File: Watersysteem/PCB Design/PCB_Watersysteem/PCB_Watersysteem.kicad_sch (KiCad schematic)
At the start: 69 parts, among them J1 12V ingang, J10 LED Water Level, J11 LED Nutrient Level, J12 Height Nutrients, J13 Height Mixer, J2 TTL Connector, J21 Voedingstoffen 1, J3 ReferentieProbe, J4 Voedingstoffen 2, J5 Voedingstoffen 3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

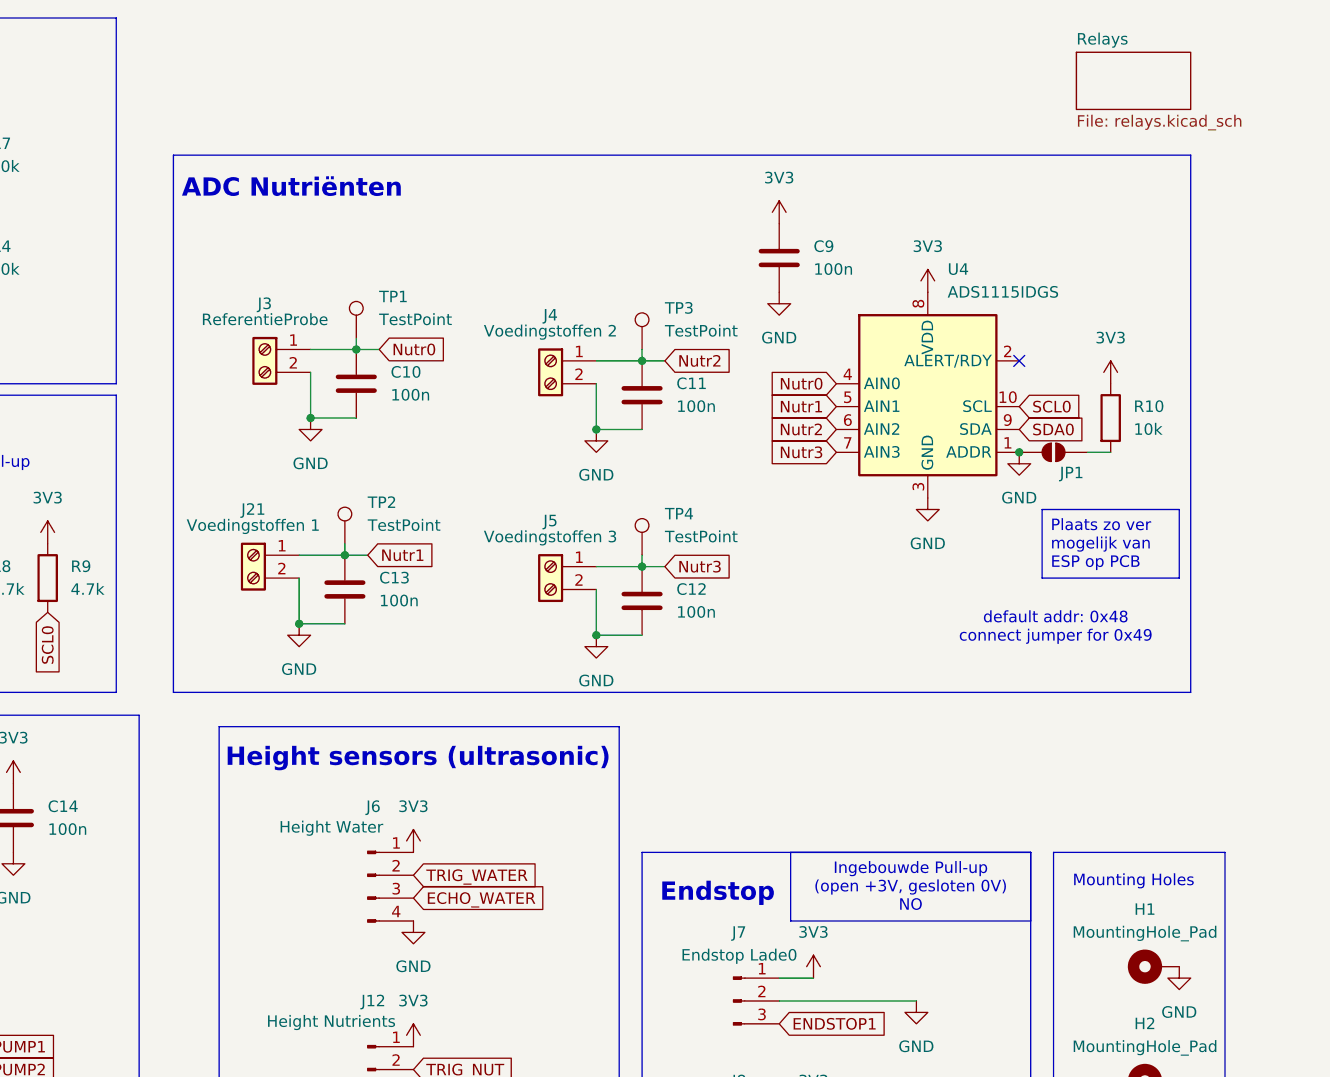
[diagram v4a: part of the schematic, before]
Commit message: Update PCB
BNC Connectoren ingevoegd, extra footprints
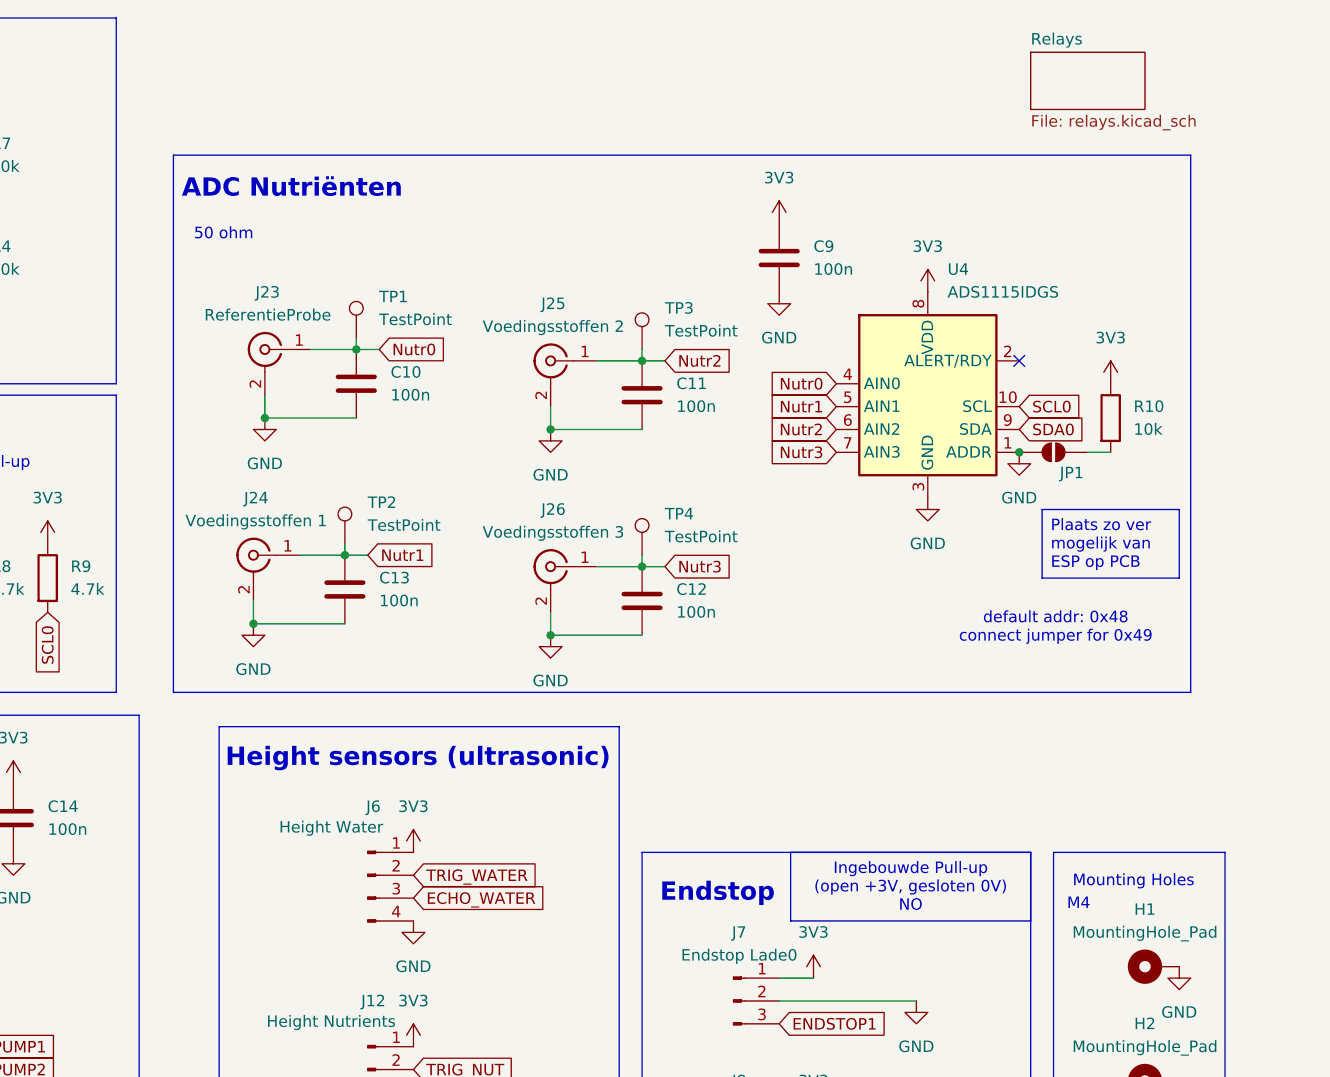
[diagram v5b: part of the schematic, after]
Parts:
- removed J21: Voedingstoffen 1, symbol Connector:Screw_Terminal_01x02
- removed J3: ReferentieProbe, symbol Connector:Screw_Terminal_01x02
- removed J4: Voedingstoffen 2, symbol Connector:Screw_Terminal_01x02
- removed J5: Voedingstoffen 3, symbol Connector:Screw_Terminal_01x02
- added J23: ReferentieProbe, Connector_Coaxial:BNC_Amphenol_B6252HB-NPP3G-50_Horizontal, symbol Connector:Conn_Coaxial
- added J24: Voedingsstoffen 1, Connector_Coaxial:BNC_Amphenol_B6252HB-NPP3G-50_Horizontal, symbol Connector:Conn_Coaxial
- added J25: Voedingsstoffen 2, Connector_Coaxial:BNC_Amphenol_B6252HB-NPP3G-50_Horizontal, symbol Connector:Conn_Coaxial
- added J26: Voedingsstoffen 3, Connector_Coaxial:BNC_Amphenol_B6252HB-NPP3G-50_Horizontal, symbol Connector:Conn_Coaxial
- C1, C2: footprint (none) -> Capacitor_SMD:CP_Elec_6.3x3.9
- C4: footprint (none) -> Capacitor_Tantalum_SMD:CP_EIA-3528-12_Kemet-T_Pad1.50x2.35mm_HandSolder
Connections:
- net GND: now also J23.2 (Ext), J24.2 (Ext), J25.2 (Ext), J26.2 (Ext)
- net Nutr0: now also J23.1 (In)
- net Nutr1: now also J24.1 (In)
- net Nutr2: now also J25.1 (In)
- net Nutr3: now also J26.1 (In)
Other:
- note added: "50 ohm"
- note added: "M4"

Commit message: Update PCB
alle footprints staan correct, alles in PCB geïmporteert
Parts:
- H1, H2, H3, H4: footprint MountingHole:MountingHole_4.3mm_M4_DIN965_Pad_TopBottom -> MountingHole:MountingHole_3.2mm_M3_Pad_TopBottom
- J1: footprint (none) -> TerminalBlock_Phoenix:TerminalBlock_Phoenix_PT-1,5-2-5.0-H_1x02_P5.00mm_Horizontal
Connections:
- net 12V: now also U2.2 (IN+); no longer U2.3 (IN+), U2.4 (IN+)
- net 5V: now also U2.3 (OUT+); no longer U2.5 (OUT+), U2.6 (OUT+)
- net GND: now also U2.4 (OUT-); no longer U2.2 (IN-), U2.7 (OUT-), U2.8 (OUT-)
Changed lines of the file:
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@@
 	)
 	(junction
+		(at 72.39 177.8)
+		(diameter 0)
+		(color 0 0 0 0)
+	)
+	(junction
 		(at 128.27 177.8)
 		(diameter 0)
@@
 	)
 	(junction
-		(at 53.34 186.69)
-		(diameter 0)
-		(color 0 0 0 0)
-	)
-	(junction
 		(at 92.71 133.35)
 		(diameter 0)
@@
 	)
 	(junction
-		(at 71.12 177.8)
-		(diameter 0)
-		(color 0 0 0 0)
-	)
-	(junction
 		(at 130.81 177.8)
 		(diameter 0)
@@
 	)
 	(junction
-		(at 71.12 186.69)
-		(diameter 0)
-		(color 0 0 0 0)
-	)
-	(junction
 		(at 187.96 50.8)
 		(diameter 0)
@@
 	)
 	(junction
-		(at 53.34 177.8)
-		(diameter 0)
-		(color 0 0 0 0)
-	)
-	(junction
 		(at 113.03 35.56)
 		(diameter 0)
@@
 		(color 0 0 0 0)
 	)
-	(junction
-		(at 73.66 177.8)
-		(diameter 0)
-		(color 0 0 0 0)
-	)
 	(no_connect
 		(at 63.5 60.96)
@@
 	(wire
 		(pts
-			(xy 73.66 177.8) (xy 74.93 177.8)
-		)
-		(stroke
-			(width 0)
-			(type default)
-		)
-	)
-	(wire
-		(pts
 			(xy 82.55 177.8) (xy 77.47 177.8)
 		)
@@
 	(wire
 		(pts
-			(xy 71.12 177.8) (xy 71.12 180.34)
-		)
-		(stroke
-			(width 0)
-			(type default)
-		)
-	)
-	(wire
-		(pts
 			(xy 234.95 139.7) (xy 250.19 139.7)
 		)
@@
 	(wire
 		(pts
-			(xy 71.12 184.15) (xy 71.12 186.69)
-		)
-		(stroke
-			(width 0)
-			(type default)
-		)
-	)
-	(wire
-		(pts
 			(xy 96.52 154.94) (xy 100.33 154.94)
 		)
@@
 	(wire
 		(pts
-			(xy 53.34 177.8) (xy 53.34 180.34)
-		)
-		(stroke
-			(width 0)
-			(type default)
-		)
-	)
-	(wire
-		(pts
 			(xy 187.96 49.53) (xy 187.96 50.8)
 		)
@@
 	(wire
 		(pts
+			(xy 71.12 184.15) (xy 71.12 186.69)
+		)
+		(stroke
+			(width 0)
+			(type default)
+		)
+	)
+	(wire
+		(pts
 			(xy 92.71 128.27) (xy 104.14 128.27)
 		)
@@
 	(wire
 		(pts
-			(xy 71.12 177.8) (xy 73.66 177.8)
+			(xy 71.12 177.8) (xy 72.39 177.8)
+		)
+		(stroke
+			(width 0)
+			(type default)
+		)
+	)
+	(wire
+		(pts
+			(xy 72.39 177.8) (xy 74.93 177.8)
 		)
 		(stroke
@@
 	)
 	(symbol
-		(lib_id "power:PWR_FLAG")
-		(at 29.21 184.15 90)
-		(unit 1)
-		(exclude_from_sim no)
-		(in_bom yes)
-		(on_board yes)
-		(dnp no)
-		(fields_autoplaced yes)
-		(property "Reference" "#FLG01"
-			(at 27.305 184.15 0)
-			(effects
-				(font
-					(size 1.27 1.27)
-				)
-				(hide yes)
-			)
-		)
-		(property "Value" "PWR_FLAG"
-			(at 25.4 184.1499 90)
-			(effects
-				(font
-					(size 1.27 1.27)
-				)
-				(justify left)
-			)
-		)
-		(property "Footprint" ""
-			(at 29.21 184.15 0)
-			(effects
-				(font
-					(size 1.27 1.27)
-				)
-				(hide yes)
-			)
-		)
-		(property "Datasheet" "~"
-			(at 29.21 184.15 0)
-			(effects
-				(font
-					(size 1.27 1.27)
-				)
-				(hide yes)
-			)
-		)
-		(property "Description" "Special symbol for telling ERC where power comes from"
-			(at 29.21 184.15 0)
-			(effects
-				(font
-					(size 1.27 1.27)
-				)
-				(hide yes)
-			)
-		)
-		(pin "1"
-		)
-		(instances
-			(project ""
-				(path "/de0b8b90-8fde-4ab1-b1b1-e85d44454ecd"
-					(reference "#FLG01")
-					(unit 1)
-				)
-			)
-		)
-	)
-	(symbol
 		(lib_id "power:GND")
 		(at 19.05 35.56 0)
@@
 			)
 		)
-		(property "Footprint" "MountingHole:MountingHole_4.3mm_M4_DIN965_Pad_TopBottom"
+		(property "Footprint" "MountingHole:MountingHole_3.2mm_M3_Pad_TopBottom"
 			(at 276.86 144.78 0)
 			(effects
@@
 	(symbol
 		(lib_id "power:VCC")
-		(at 73.66 177.8 0)
+		(at 72.39 177.8 0)
 		(unit 1)
 		(exclude_from_sim no)
@@
 		(fields_autoplaced yes)
 		(property "Reference" "#PWR06"
-			(at 73.66 181.61 0)
+			(at 72.39 181.61 0)
 			(effects
 				(font
@@
 		)
 		(property "Value" "5V"
-			(at 73.66 172.72 0)
+			(at 72.39 172.72 0)
 			(effects
 				(font
@@
 		)
 		(property "Footprint" ""
-			(at 73.66 177.8 0)
+			(at 72.39 177.8 0)
 			(effects
 				(font
@@
 		)
 		(property "Datasheet" ""
-			(at 73.66 177.8 0)
+			(at 72.39 177.8 0)
 			(effects
 				(font
@@
 		)
 		(property "Description" "Power symbol creates a global label with name \"VCC\""
-			(at 73.66 177.8 0)
+			(at 72.39 177.8 0)
 			(effects
 				(font
@@
 			)
 		)
+		(property "Sim.Pins" "1=K 2=A"
+			(at 148.59 177.8 0)
+			(effects
+				(font
+					(size 1.27 1.27)
+				)
+				(hide yes)
+			)
+		)
 		(pin "2"
 		)
@@
 	)
 	(symbol
+		(lib_name "LED_1")
 		(lib_id "Device:LED")
 		(at 130.81 78.74 90)
@@
 			)
 		)
+		(property "Sim.Pins" "1=K 2=A"
+			(at 130.81 78.74 0)
+			(effects
+				(font
+					(size 1.27 1.27)
+				)
+				(hide yes)
+			)
+		)
 		(pin "2"
 		)
@@
 			)
 		)
-		(property "Footprint" "MountingHole:MountingHole_4.3mm_M4_DIN965_Pad_TopBottom"
+		(property "Footprint" "MountingHole:MountingHole_3.2mm_M3_Pad_TopBottom"
 			(at 276.86 158.75 0)
 			(effects
@@
 			)
 		)
-		(property "Footprint" "MountingHole:MountingHole_4.3mm_M4_DIN965_Pad_TopBottom"
+		(property "Footprint" "MountingHole:MountingHole_3.2mm_M3_Pad_TopBottom"
 			(at 276.86 132.08 0)
 			(effects
@@
 	(symbol
 		(lib_id "Watersysteem_Library:MP1584_Module")
-		(at 62.23 181.61 0)
+		(at 62.23 180.34 0)
 		(unit 1)
 		(exclude_from_sim no)
@@
 		(fields_autoplaced yes)
 		(property "Reference" "U2"
-			(at 62.23 171.45 0)
+			(at 62.23 170.18 0)
 			(effects
 				(font
@@
 		)
 		(property "Value" "MP1584_Module"
-			(at 62.23 173.99 0)
+			(at 62.23 172.72 0)
 			(effects
 				(font
@@
 		)
 		(property "Footprint" "Watersysteem_Footprints_Library:MP1584_Module"
-			(at 62.23 172.212 0)
+			(at 62.23 170.942 0)
 			(effects
 				(font
@@
 		)
 		(property "Datasheet" ""
-			(at 62.23 172.212 0)
+			(at 62.23 170.942 0)
 			(effects
 				(font
@@
 		)
 		(property "Description" ""
-			(at 62.23 172.212 0)
+			(at 62.23 170.942 0)
 			(effects
 				(font
@@
 		(pin "2"
 		)
-		(pin "3"
-		)
-		(pin "6"
-		)
-		(pin "5"
-		)
 		(pin "4"
 		)
-		(pin "8"
-		)
-		(pin "7"
+		(pin "3"
 		)
 		(instances
@@
 			)
 		)
-		(property "Footprint" "MountingHole:MountingHole_4.3mm_M4_DIN965_Pad_TopBottom"
+		(property "Footprint" "MountingHole:MountingHole_3.2mm_M3_Pad_TopBottom"
 			(at 276.86 119.38 0)
 			(effects
@@
 			)
 		)
-		(property "Footprint" ""
+		(property "Footprint" "TerminalBlock_Phoenix:TerminalBlock_Phoenix_PT-1,5-2-5.0-H_1x02_P5.00mm_Horizontal"
 			(at 24.13 177.8 0)
 			(effects

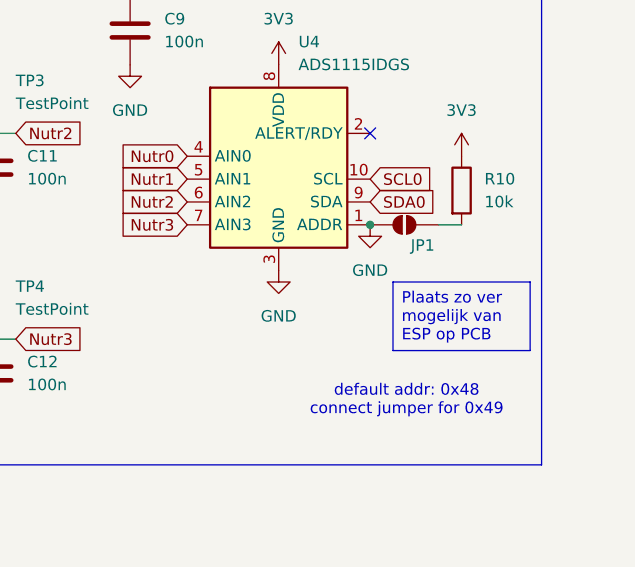
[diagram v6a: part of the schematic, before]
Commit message: componenten gegroepeerd
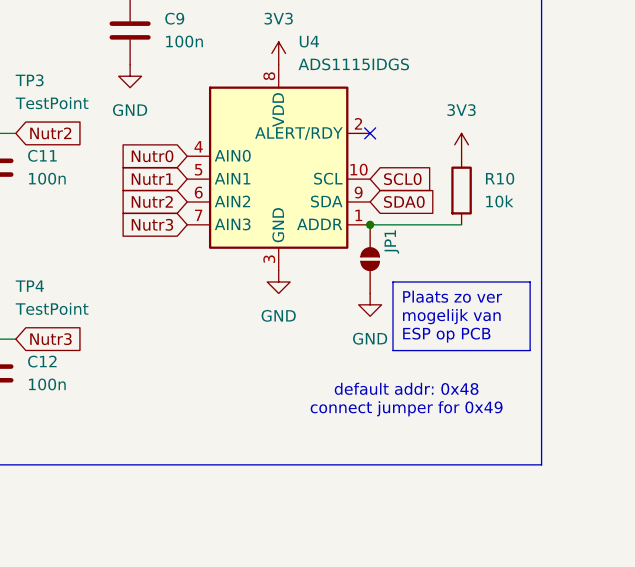
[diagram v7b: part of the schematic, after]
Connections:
- net GND: no longer U4.1 (ADDR)
- net at JP1.2 (B), R10.2: now also U4.1 (ADDR)
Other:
- moved on the sheet: JP1
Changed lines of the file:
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@@
 	)
 	(junction
-		(at 92.71 154.94)
+		(at 261.62 62.23)
 		(diameter 0)
 		(color 0 0 0 0)
 	)
 	(junction
-		(at 77.47 177.8)
+		(at 92.71 154.94)
 		(diameter 0)
 		(color 0 0 0 0)
 	)
 	(junction
-		(at 100.33 140.97)
+		(at 77.47 177.8)
 		(diameter 0)
 		(color 0 0 0 0)
 	)
 	(junction
-		(at 261.62 62.23)
+		(at 100.33 140.97)
 		(diameter 0)
 		(color 0 0 0 0)
@@
 	(wire
 		(pts
-			(xy 271.78 62.23) (xy 269.24 62.23)
-		)
-		(stroke
-			(width 0)
-			(type default)
-		)
-	)
-	(wire
-		(pts
 			(xy 74.93 177.8) (xy 77.47 177.8)
 		)
@@
 	(wire
 		(pts
+			(xy 261.62 62.23) (xy 271.78 62.23)
+		)
+		(stroke
+			(width 0)
+			(type default)
+		)
+	)
+	(wire
+		(pts
 			(xy 234.95 153.67) (xy 237.49 153.67)
 		)
@@
 	(symbol
 		(lib_id "Jumper:SolderJumper_2_Open")
-		(at 265.43 62.23 0)
+		(at 261.62 66.04 90)
 		(unit 1)
 		(exclude_from_sim no)
@@
 		(dnp no)
 		(property "Reference" "JP1"
-			(at 267.462 64.516 0)
+			(at 263.906 64.008 0)
 			(effects
 				(font
@@
 		)
 		(property "Value" "SolderJumper_2_Open"
-			(at 265.43 58.42 0)
+			(at 257.81 66.04 0)
 			(effects
 				(font
@@
 		)
 		(property "Footprint" "Jumper:SolderJumper-2_P1.3mm_Open_RoundedPad1.0x1.5mm"
-			(at 265.43 62.23 0)
+			(at 261.62 66.04 0)
 			(effects
 				(font
@@
 		)
 		(property "Datasheet" "~"
-			(at 265.43 62.23 0)
+			(at 261.62 66.04 0)
 			(effects
 				(font
@@
 		)
 		(property "Description" "Solder Jumper, 2-pole, open"
-			(at 265.43 62.23 0)
+			(at 261.62 66.04 0)
 			(effects
 				(font
@@
 	(symbol
 		(lib_id "power:GND")
-		(at 261.62 62.23 0)
+		(at 261.62 69.85 0)
 		(unit 1)
 		(exclude_from_sim no)
@@
 		(fields_autoplaced yes)
 		(property "Reference" "#PWR049"
-			(at 261.62 68.58 0)
+			(at 261.62 76.2 0)
 			(effects
 				(font
@@
 		)
 		(property "Value" "GND"
-			(at 261.62 67.31 0)
+			(at 261.62 74.93 0)
 			(effects
 				(font
@@
 		)
 		(property "Footprint" ""
-			(at 261.62 62.23 0)
+			(at 261.62 69.85 0)
 			(effects
 				(font
@@
 		)
 		(property "Datasheet" ""
-			(at 261.62 62.23 0)
+			(at 261.62 69.85 0)
 			(effects
 				(font
@@
 		)
 		(property "Description" "Power symbol creates a global label with name \"GND\" , ground"
-			(at 261.62 62.23 0)
+			(at 261.62 69.85 0)
 			(effects
 				(font
